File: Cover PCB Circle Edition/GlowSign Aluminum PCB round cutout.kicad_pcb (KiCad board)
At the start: 2 copper layers, 175.4 x 88.4 mm, 4 parts, among them U1 SMTSO3030CTJ, U2 SMTSO3030CTJ, U3 SMTSO3030CTJ, U4 SMTSO3030CTJ

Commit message: updated cover circle pcb
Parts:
- added G***: LOGO, LOGO, F.Cu at (187.5, 76.1)
- added OSHW logo: OSHW-Logo2_7.3x6mm_SilkScreen, Symbol:OSHW-Logo2_7.3x6mm_SilkScreen, F.Cu at (201.3, 76.6)
- added P1: Thermal_Pad, footprint:Thermal pad, F.Cu at (78.1, 109.3)
- added P2: Thermal_Pad, footprint:Thermal pad, F.Cu at (78.1, 78.0)
- added P3: Thermal_Pad, footprint:Thermal pad, F.Cu at (129.6, 64.5)
- added P4: Thermal_Pad, footprint:Thermal pad, F.Cu at (227.1, 109.3)
- added P5: Thermal_Pad, footprint:Thermal pad, F.Cu at (132.7, 129.5)
- added P6: Thermal_Pad, footprint:Thermal pad, F.Cu at (227.1, 78.0)
- added logo: LOGO, LOGO, F.Cu at (188.4, 115.3)
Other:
- board text added: "Cover PCB v1.0 Circle edition"
- board text added: "GlowSign"
- board text added: "PCB files: https://bit.ly/ 3A1viPe"
- board text added: "designed by"

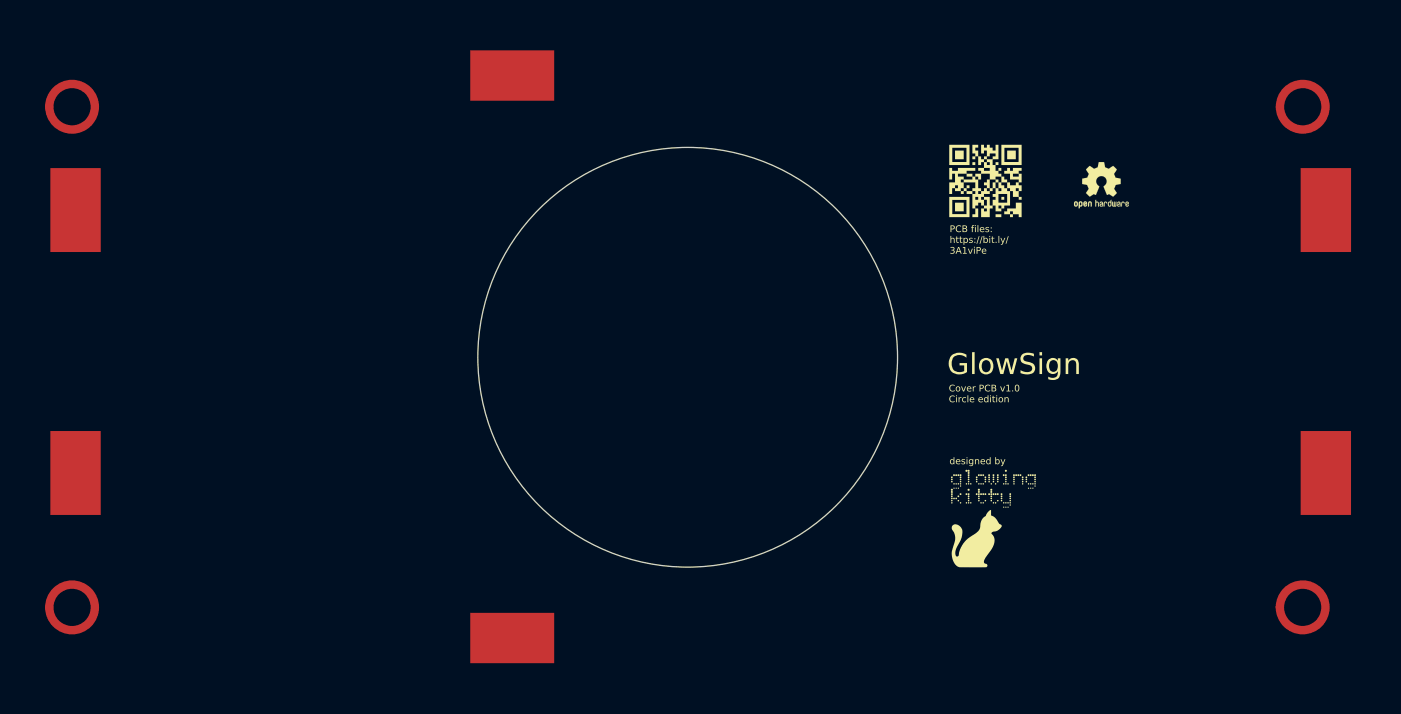
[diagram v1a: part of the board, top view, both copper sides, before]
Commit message: separated battery electronics into separate pcb
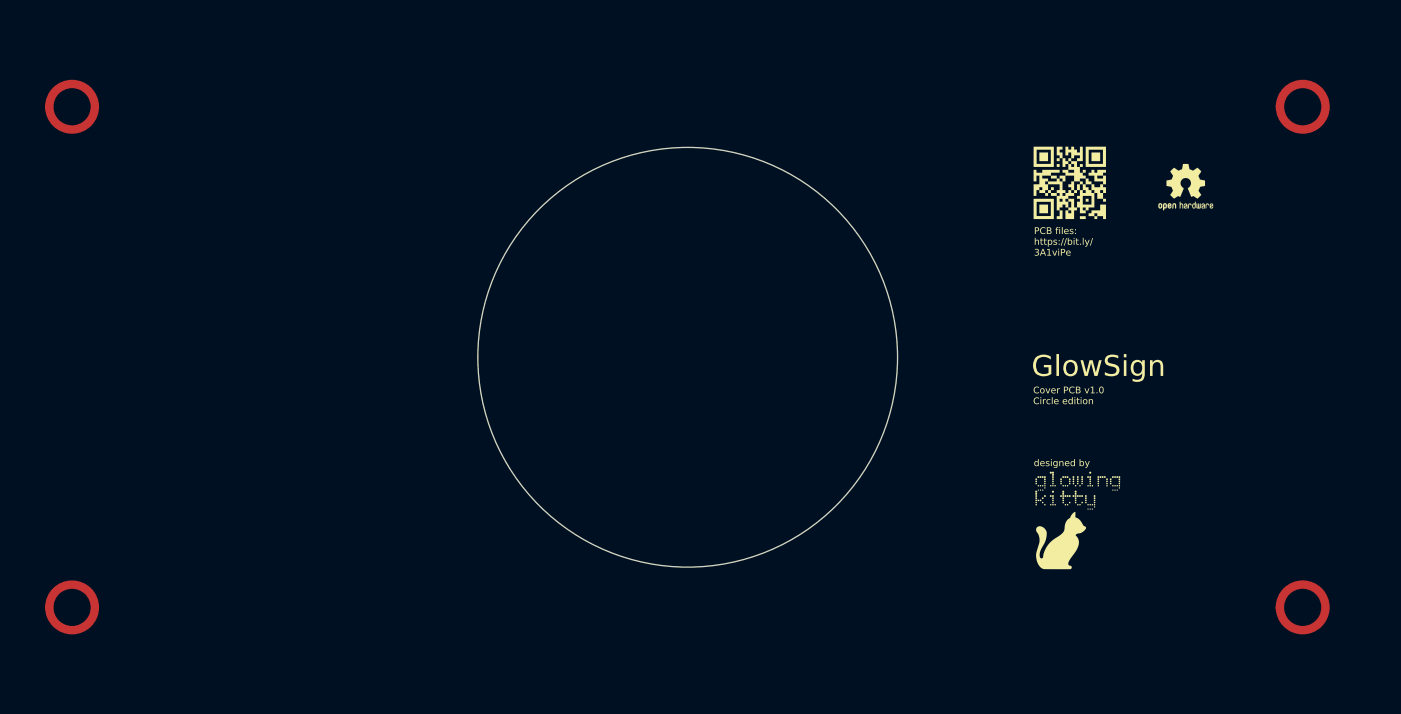
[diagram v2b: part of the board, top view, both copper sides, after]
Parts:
- removed P1, P2, P3, P4, P5, P6: Thermal_Pad, footprint:Thermal pad
- moved G*** 10.1 mm to (197.6, 76.3)
- moved OSHW logo 10.1 mm to (211.4, 76.8)
- moved logo 10.1 mm to (198.4, 115.5)
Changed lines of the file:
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@@
   (net 0 "")
   (net 1 "GND")
-  (footprint "footprint:Thermal pad" (layer "F.Cu")
-    (at 227.086952 78.005352)
-    (property "Sheetfile" "GlowSign Aluminum CB square cutout.kicad_sch")
-    (property "Sheetname" "")
-    (property "exclude_from_bom" "")
-    (attr exclude_from_bom)
-    (fp_text reference "P6" (at 0.91 -2.65 unlocked) (layer "F.SilkS") hide
-      (effects (font (size 1 1) (thickness 0.15)))
-    )
-    (fp_text value "Thermal_Pad" (at 0.48 5.74 unlocked) (layer "F.Fab")
-      (effects (font (size 1 1) (thickness 0.15)))
-    )
-    (fp_text user "${REFERENCE}" (at 0.48 7.24 unlocked) (layer "F.Fab")
-      (effects (font (size 1 1) (thickness 0.15)))
-    )
-    (pad "1" smd rect (at 0.9819 1.5354) (size 6 10) (layers "F.Cu" "F.Mask")
-      (net 1 "GND") (pintype "bidirectional"))
-  )
   (footprint "LOGO" (layer "F.Cu")
-    (at 187.513752 76.074952)
+    (at 197.5612 76.3016)
     (attr board_only exclude_from_pos_files exclude_from_bom)
     (fp_text reference "G***" (at 0 0) (layer "F.SilkS") hide
@@
       ) (layer "F.SilkS") (width 0) (fill solid))
   )
-  (footprint "footprint:Thermal pad" (layer "F.Cu")
-    (at 227.085452 109.327835)
-    (property "Sheetfile" "GlowSign Aluminum CB square cutout.kicad_sch")
-    (property "Sheetname" "")
-    (property "exclude_from_bom" "")
-    (attr exclude_from_bom)
-    (fp_text reference "P4" (at 0.91 -2.65 unlocked) (layer "F.SilkS") hide
-      (effects (font (size 1 1) (thickness 0.15)))
-    )
-    (fp_text value "Thermal_Pad" (at 0.48 5.74 unlocked) (layer "F.Fab")
-      (effects (font (size 1 1) (thickness 0.15)))
-    )
-    (fp_text user "${REFERENCE}" (at 0.48 7.24 unlocked) (layer "F.Fab")
-      (effects (font (size 1 1) (thickness 0.15)))
-    )
-    (pad "1" smd rect (at 0.9819 1.5354) (size 6 10) (layers "F.Cu" "F.Mask")
-      (net 1 "GND") (pintype "bidirectional"))
-  )
-  (footprint "footprint:Thermal pad" (layer "F.Cu")
-    (at 78.139852 109.327835)
-    (property "Sheetfile" "GlowSign Aluminum CB square cutout.kicad_sch")
-    (property "Sheetname" "")
-    (property "exclude_from_bom" "")
-    (attr exclude_from_bom)
-    (fp_text reference "P1" (at 0.91 -2.65 unlocked) (layer "F.SilkS") hide
-      (effects (font (size 1 1) (thickness 0.15)))
-    )
-    (fp_text value "Thermal_Pad" (at 0.48 5.74 unlocked) (layer "F.Fab")
-      (effects (font (size 1 1) (thickness 0.15)))
-    )
-    (fp_text user "${REFERENCE}" (at 0.48 7.24 unlocked) (layer "F.Fab")
-      (effects (font (size 1 1) (thickness 0.15)))
-    )
-    (pad "1" smd rect (at 0.9819 1.5354) (size 6 10) (layers "F.Cu" "F.Mask")
-      (net 1 "GND") (pintype "bidirectional"))
-  )
   (footprint "footprint:SMTSO3030CTJ No hole" (layer "F.Cu")
     (at 78.700152 126.874952)
@@
     )
   )
-  (footprint "footprint:Thermal pad" (layer "F.Cu")
-    (at 129.605552 64.499535 90)
-    (property "Sheetfile" "GlowSign Aluminum CB square cutout.kicad_sch")
-    (property "Sheetname" "")
-    (property "exclude_from_bom" "")
-    (attr exclude_from_bom)
-    (fp_text reference "P3" (at 0.91 -2.65 90 unlocked) (layer "F.SilkS") hide
-      (effects (font (size 1 1) (thickness 0.15)))
-    )
-    (fp_text value "Thermal_Pad" (at 0.48 5.74 90 unlocked) (layer "F.Fab")
-      (effects (font (size 1 1) (thickness 0.15)))
-    )
-    (fp_text user "${REFERENCE}" (at 0.48 7.24 90 unlocked) (layer "F.Fab")
-      (effects (font (size 1 1) (thickness 0.15)))
-    )
-    (pad "1" smd rect (at 0.9819 1.5354 90) (size 6 10) (layers "F.Cu" "F.Mask")
-      (net 1 "GND") (pintype "bidirectional"))
-  )
-  (footprint "footprint:Thermal pad" (layer "F.Cu")
-    (at 132.676352 129.540935 -90)
-    (property "Sheetfile" "GlowSign Aluminum CB square cutout.kicad_sch")
-    (property "Sheetname" "")
-    (property "exclude_from_bom" "")
-    (attr exclude_from_bom)
-    (fp_text reference "P5" (at 0.91 -2.65 -90 unlocked) (layer "F.SilkS") hide
-      (effects (font (size 1 1) (thickness 0.15)))
-    )
-    (fp_text value "Thermal_Pad" (at 0.48 5.74 -90 unlocked) (layer "F.Fab")
-      (effects (font (size 1 1) (thickness 0.15)))
-    )
-    (fp_text user "${REFERENCE}" (at 0.48 7.24 -90 unlocked) (layer "F.Fab")
-      (effects (font (size 1 1) (thickness 0.15)))
-    )
-    (pad "1" smd rect (at 0.9819 1.5354 270) (size 6 10) (layers "F.Cu" "F.Mask")
-      (net 1 "GND") (pintype "bidirectional"))
-  )
   (footprint "footprint:SMTSO3030CTJ No hole" (layer "F.Cu")
     (at 78.700152 67.235752)
@@
     )
   )
-  (footprint "footprint:Thermal pad" (layer "F.Cu")
-    (at 78.141352 78.005352)
-    (property "Sheetfile" "GlowSign Aluminum CB square cutout.kicad_sch")
-    (property "Sheetname" "")
-    (property "exclude_from_bom" "")
-    (attr exclude_from_bom)
-    (fp_text reference "P2" (at 0.91 -2.65 unlocked) (layer "F.SilkS") hide
-      (effects (font (size 1 1) (thickness 0.15)))
-    )
-    (fp_text value "Thermal_Pad" (at 0.48 5.74 unlocked) (layer "F.Fab")
-      (effects (font (size 1 1) (thickness 0.15)))
-    )
-    (fp_text user "${REFERENCE}" (at 0.48 7.24 unlocked) (layer "F.Fab")
-      (effects (font (size 1 1) (thickness 0.15)))
-    )
-    (pad "1" smd rect (at 0.9819 1.5354) (size 6 10) (layers "F.Cu" "F.Mask")
-      (net 1 "GND") (pintype "bidirectional"))
-  )
   (footprint "footprint:SMTSO3030CTJ No hole" (layer "F.Cu")
     (at 225.308952 67.235752)
@@
   )
   (footprint "Symbol:OSHW-Logo2_7.3x6mm_SilkScreen" (layer "F.Cu")
-    (at 201.331352 76.582952)
+    (at 211.3788 76.8096)
     (descr "Open Source Hardware Symbol")
     (tags "Logo Symbol OSHW")
@@
   )
   (footprint "LOGO" (layer "F.Cu")
-    (at 188.377352 115.292552)
+    (at 198.4248 115.5192)
     (attr board_only exclude_from_pos_files exclude_from_bom)
     (fp_text reference "logo" (at 0 0) (layer "F.SilkS") hide
@@
   (gr_circle (center 225.3128 126.8484) (end 228.8128 126.8484) (layer "User.1") (width 0.1) (fill none))
   (gr_arc (start 235.5128 52.8484) (mid 238.482613 54.078587) (end 239.7128 57.0484) (layer "User.1") (width 0.1))
-  (gr_text "Cover PCB v1.0\nCircle edition" (at 183.144952 101.424152) (layer "F.SilkS")
+  (gr_text "Cover PCB v1.0\nCircle edition" (at 193.1924 101.6508) (layer "F.SilkS")
     (effects (font (size 0.8 0.8) (thickness 0.15)) (justify left))
   )
-  (gr_text "designed by" (at 183.221152 109.450552) (layer "F.SilkS")
+  (gr_text "designed by" (at 193.2686 109.6772) (layer "F.SilkS")
     (effects (font (size 0.8 0.8) (thickness 0.15)) (justify left))
   )
-  (gr_text "PCB files:\nhttps://bit.ly/\n3A1viPe" (at 183.246552 83.085352) (layer "F.SilkS")
+  (gr_text "PCB files:\nhttps://bit.ly/\n3A1viPe" (at 193.294 83.312) (layer "F.SilkS")
     (effects (font (size 0.8 0.8) (thickness 0.15)) (justify left))
   )
-  (gr_text "GlowSign" (at 182.941752 97.918952) (layer "F.SilkS")
+  (gr_text "GlowSign" (at 192.9892 98.1456) (layer "F.SilkS")
     (effects (font (size 2.5 2.5) (thickness 0.4)) (justify left))
   )
